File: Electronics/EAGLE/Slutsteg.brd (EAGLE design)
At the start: 100 x 160 mm, 167 parts, among them CN1 OSTYK33102030-2, CN2 OSTYK33102030-2, CN3 OSTYK33102030-2, IC1 SPX1117M3-L-3-3_TR, IC10 LM324D, IC11 L78M12ABDT-TR, IC2 L78M12ABDT-TR, IC3 ESP32-WROVER-IE-4MB, IC4 TM8211, IC5 LM324D, IC6 TPA3244DDWR, IC7 TPA3251D2DDVR, IC8 LM324D, IC9 LM324D, J1 0532610671, J2 JW-PJ-307-4H, J4 B4P-VH_LF__SN_, SW3 PDB181-K420F-103A2

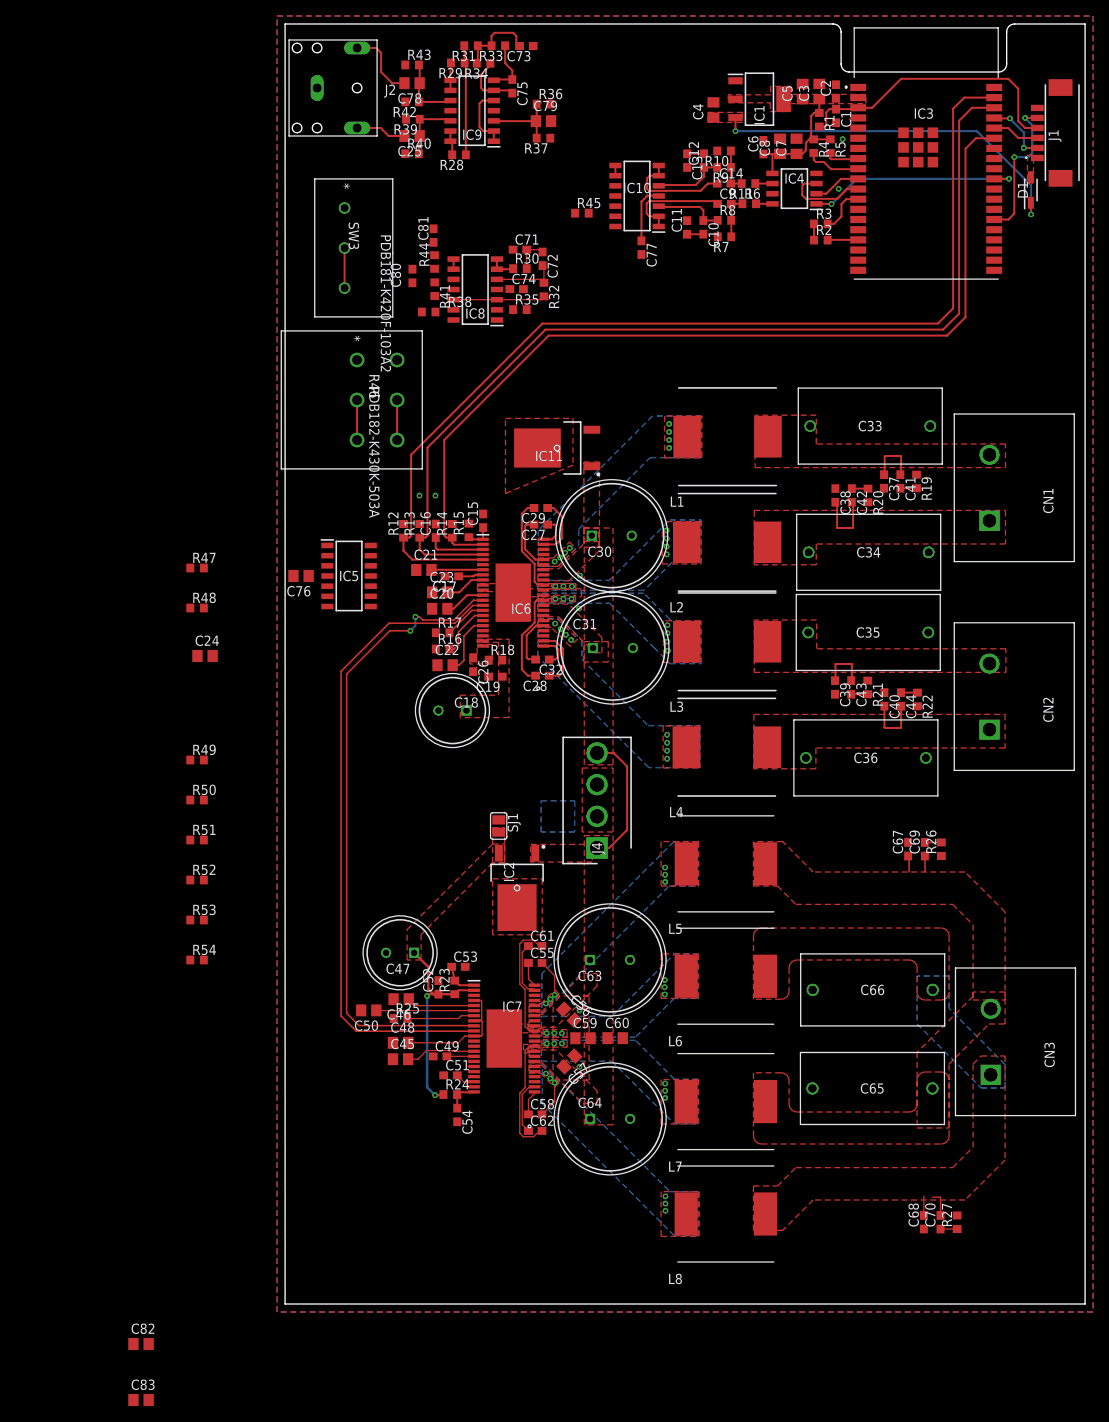
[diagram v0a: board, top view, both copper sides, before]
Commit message: Almost done with first draft of layout.
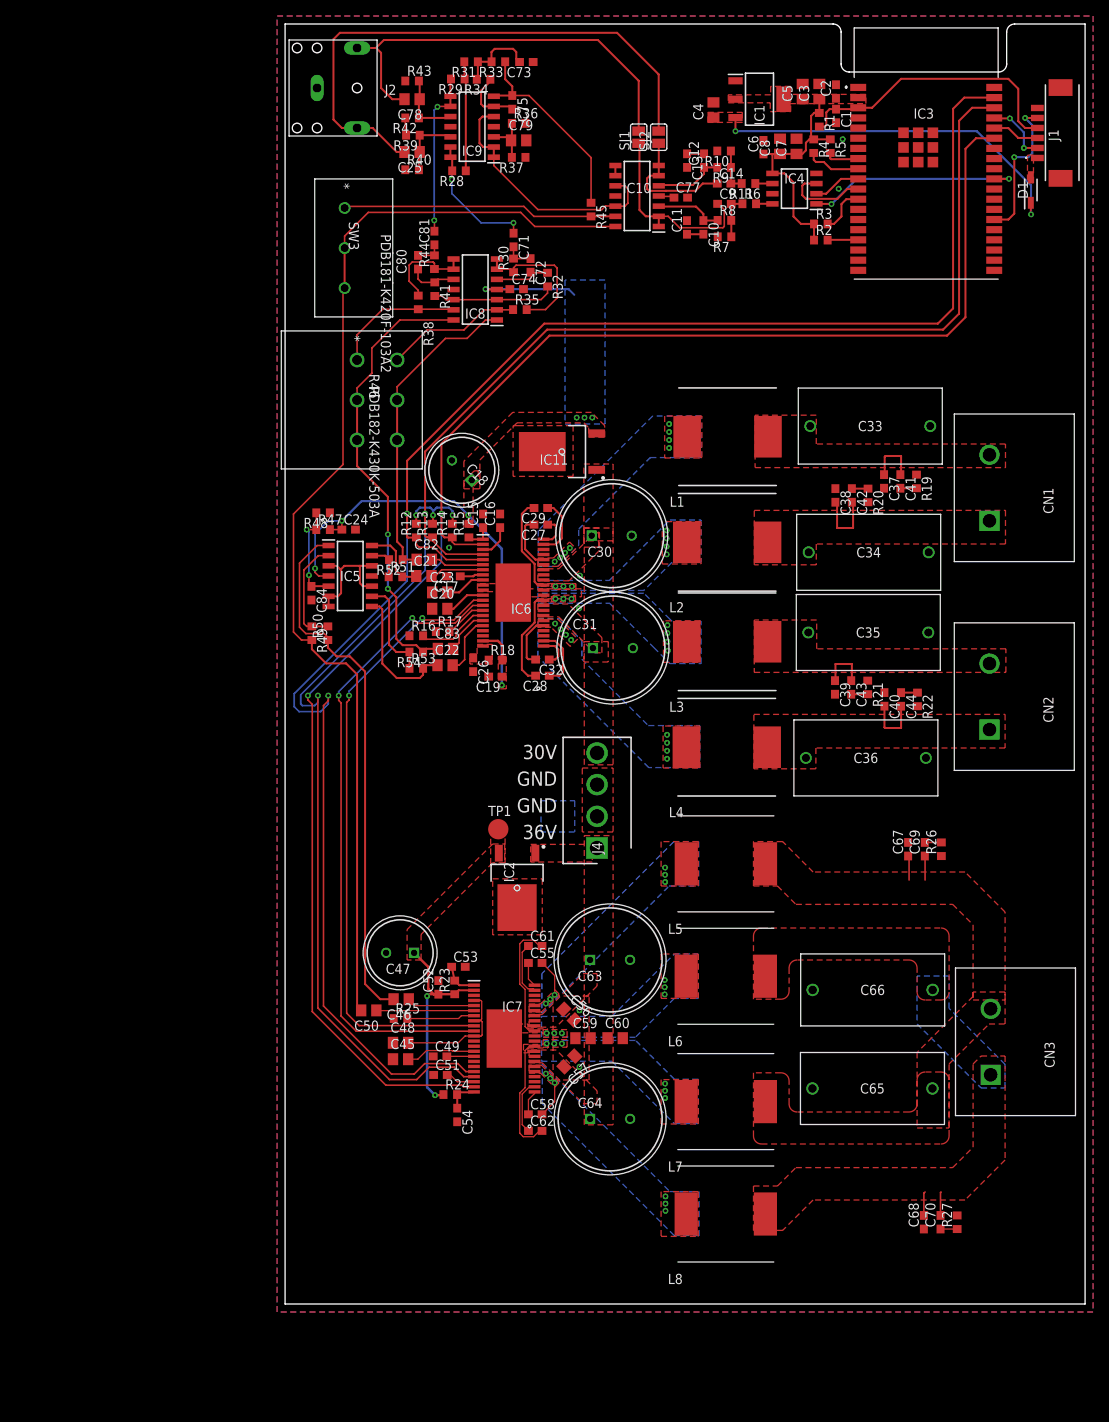
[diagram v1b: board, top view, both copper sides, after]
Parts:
- removed C76: 1uF/50V, rcl:C0805
- added C84: 100nF/50V, rcl:C0603
- added SJ2: (no value), jumper:SJ
- added TP1: TPB2,54, testpad:B2,54
- C24: value 1uF/50V -> 100nF/50V; device rcl:C0805 -> rcl:C0603
- moved C82 104.2 mm to (17.4, 93.0)
- moved C83 101.3 mm to (20.1, 81.9)
- moved SJ1 87.9 mm to (44.2, 145.8), turned to 90 degrees
- moved R54 47.3 mm to (16.4, 81.5), turned to 180 degrees
- moved R52 47.1 mm to (13.8, 93.0), turned to 180 degrees
- moved R53 41.7 mm to (16.4, 79.5)
- moved R51 41.2 mm to (13.8, 90.9)
- moved C18 28.8 mm to (23.3, 103.0), turned to 135 degrees
- moved R50 26.5 mm to (5.35, 83.8), turned to 90 degrees
- moved C24 23.9 mm to (7.95, 96.8)
- moved R49 21.4 mm to (3.35, 83.8), turned to 270 degrees
- moved R48 19.7 mm to (4.75, 98.9), turned to 180 degrees
- moved R47 16.5 mm to (4.75, 96.8)
- moved C16 8.15 mm to (26.9, 97.9)
- moved C77 7.96 mm to (49.5, 138.3), turned to 0 degrees
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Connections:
- removed net BASE_OUT: IC10.14, R49.2, SW3.2, SW3.3
- removed net BASE_OUT2: IC5.1, R50.1
- removed net BLE-L: C14.1, IC10.6, IC10.7
- removed net BLE-R: C9.1, IC10.1, IC10.2
- removed net LEFT_OUT: IC8.1, R46.5, R46.6, R52.1
- removed net LEFT_OUT2: IC5.14, R51.2
- removed net RIGHT_OUT: IC8.14, R46.2, R46.3, R54.1
- removed net RIGHT_OUT2: IC5.8, R53.2
- new net GSDJT: C9.1, IC10.1, IC10.2, SJ1.1
- new net PVDD2: C56.1, C57.2, C59.2, C60.1, C63.1, C64.1, IC2.1, IC7.29, IC7.30, IC7.31, IC7.36, IC7.37, IC7.38, J4.1
- new net TGHJESYRJK: C14.1, IC10.6, IC10.7, SJ2.1
- net GND: now also C84.2; no longer C76.2
- net INPUT_A: now also IC5.8, R53.2
- net INPUT_A_SLAVE: now also IC5.1, R50.1
- net INPUT_B: now also IC8.14, R46.2, R46.3, R54.1
- net INPUT_B_SLAVE: now also IC10.14, R49.2, SW3.2, SW3.3
- net INPUT_C: now also IC5.14, R51.2
- net INPUT_D: now also IC8.1, R46.5, R46.6, R52.1
- net N$6: now also C84.1; no longer C24.1
- net PVDD: no longer C56.1, C57.2, C59.2, C60.1, C63.1, C64.1, IC2.1, IC7.29, IC7.30, IC7.31, IC7.36, IC7.37, IC7.38, J4.1
- net SIG_IN_LEFT: now also SJ2.2
- net SIG_IN_RIGHT: now also SJ1.2
- net VDD: now also C24.1; no longer C76.1, SJ1.1
- net VDD2: now also TP1.TP; no longer SJ1.2
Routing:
- net INPUT_B_SLAVE: track 0.00 -> 141.0 mm
- net RESET: track 129.2 -> 225.8 mm, vias 0 -> 2
- net FAULT: track 124.3 -> 218.9 mm, vias 0 -> 2
- net CLIP_OTW: track 114.3 -> 208.1 mm, vias 0 -> 2
- net VDD: track 53.9 -> 124.9 mm, vias 2 -> 10
- net INPUT_A_SLAVE: track 0.00 -> 67.2 mm
- net SIG_IN_LEFT: track 6.34 -> 70.8 mm
- net INPUT_B: track 0.00 -> 56.9 mm, vias 0 -> 2
- net SIG_IN_RIGHT: track 9.15 -> 52.8 mm
- net INPUT_D: track 0.00 -> 39.6 mm
- net N$4: track 0.00 -> 34.4 mm
- net 6V_BUFFER: track 19.6 -> 47.6 mm
- net GSDJT: track 0.00 -> 24.5 mm
- net +3V3: track 20.4 -> 40.9 mm, vias 0 -> 3
- net BASE_VOLUME: track 6.93 -> 25.6 mm
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- added copper zone on layer 1, net PVDD2
- added copper zone on layer 16, net VDD
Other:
- board text added: "30V"
- board text added: "36V"
- board text added: "GND"

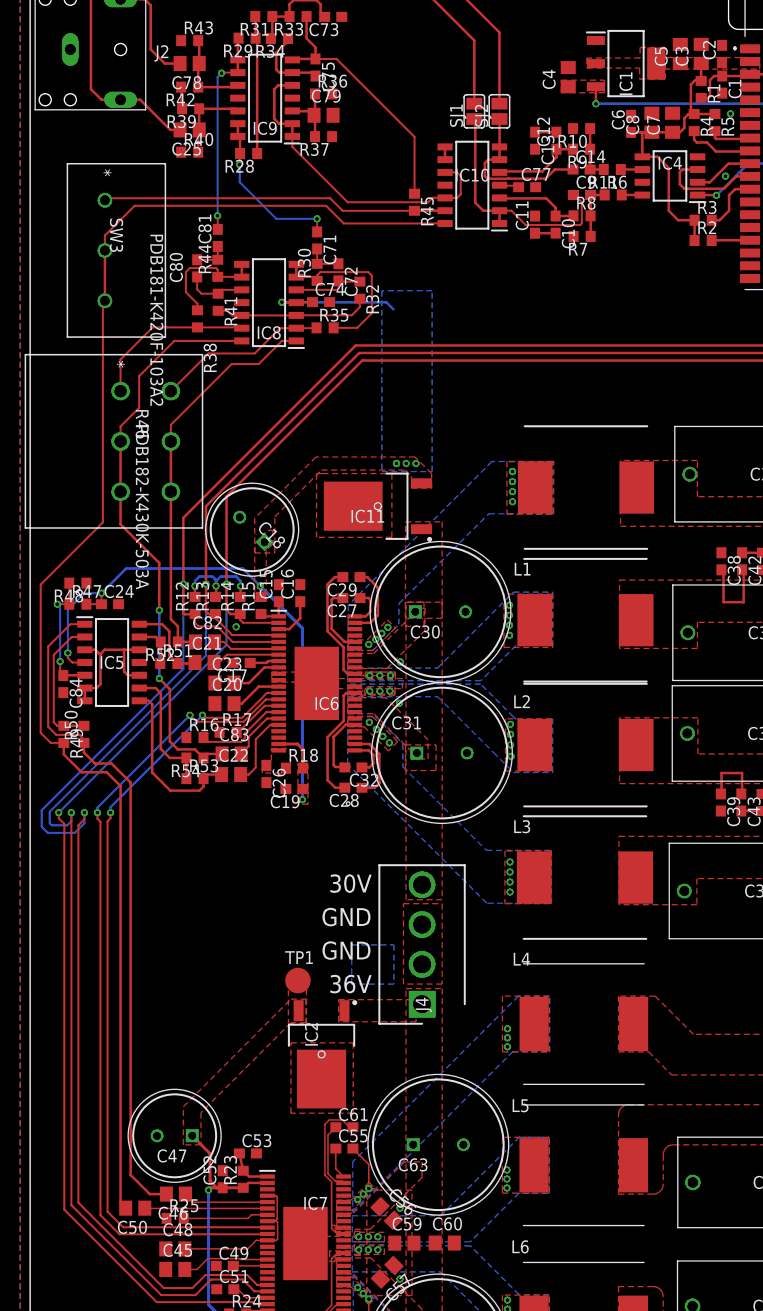
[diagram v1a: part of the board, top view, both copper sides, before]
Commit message: First draft of layout is finished. No DRC warnings.
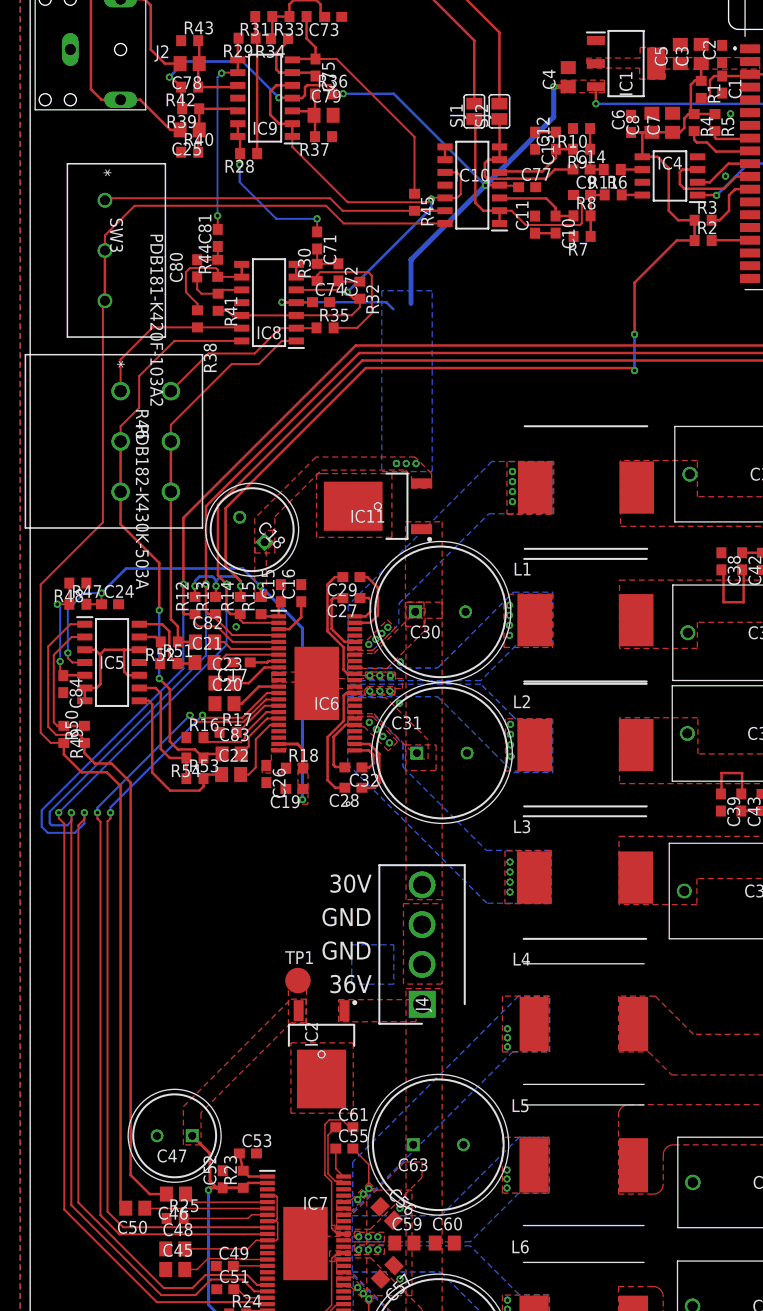
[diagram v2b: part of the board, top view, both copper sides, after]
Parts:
- moved C15 0.20 mm to (24.9, 97.9)
- moved C16 0.10 mm to (27.0, 97.9)
- moved C17 0.05 mm to (21.1, 91.0)
- moved R50 0.05 mm to (5.40, 83.8)
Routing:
- net +3V3: track 40.9 -> 112.2 mm, vias 3 -> 5
- net VDD: track 124.9 -> 195.7 mm, vias 10 -> 15
- net 6V_BUFFER: track 47.6 -> 62.3 mm, vias 0 -> 2
- net CLIP_OTW: track 208.1 -> 208.8 mm

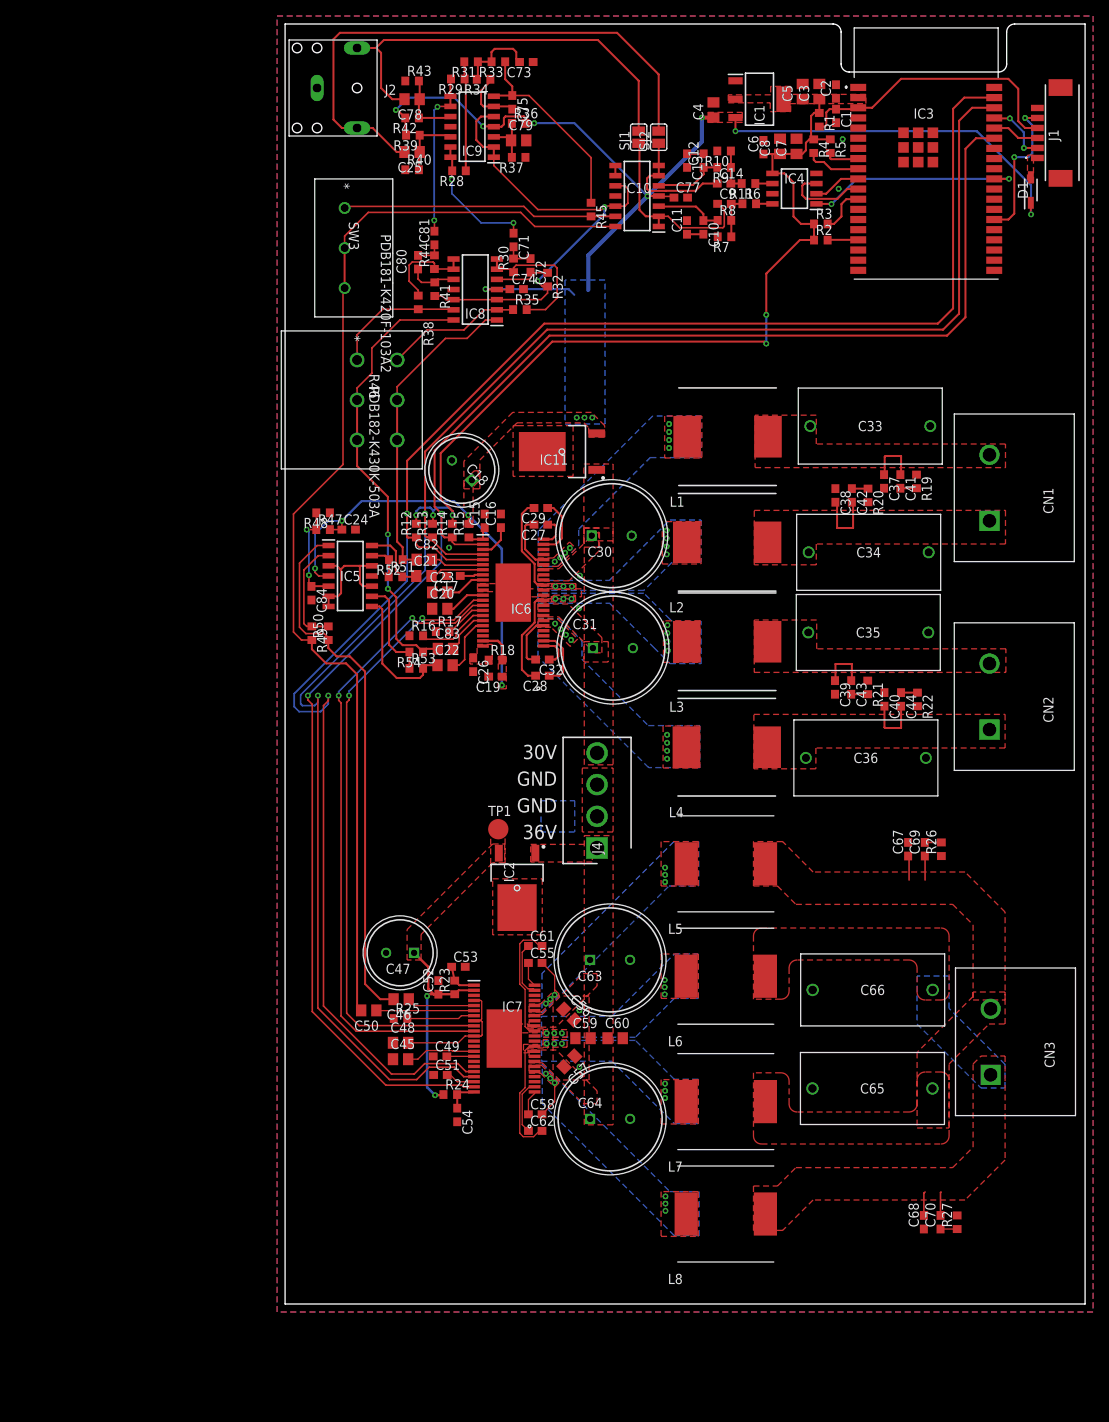
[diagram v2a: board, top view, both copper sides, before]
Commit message: Added some test points. More to come....
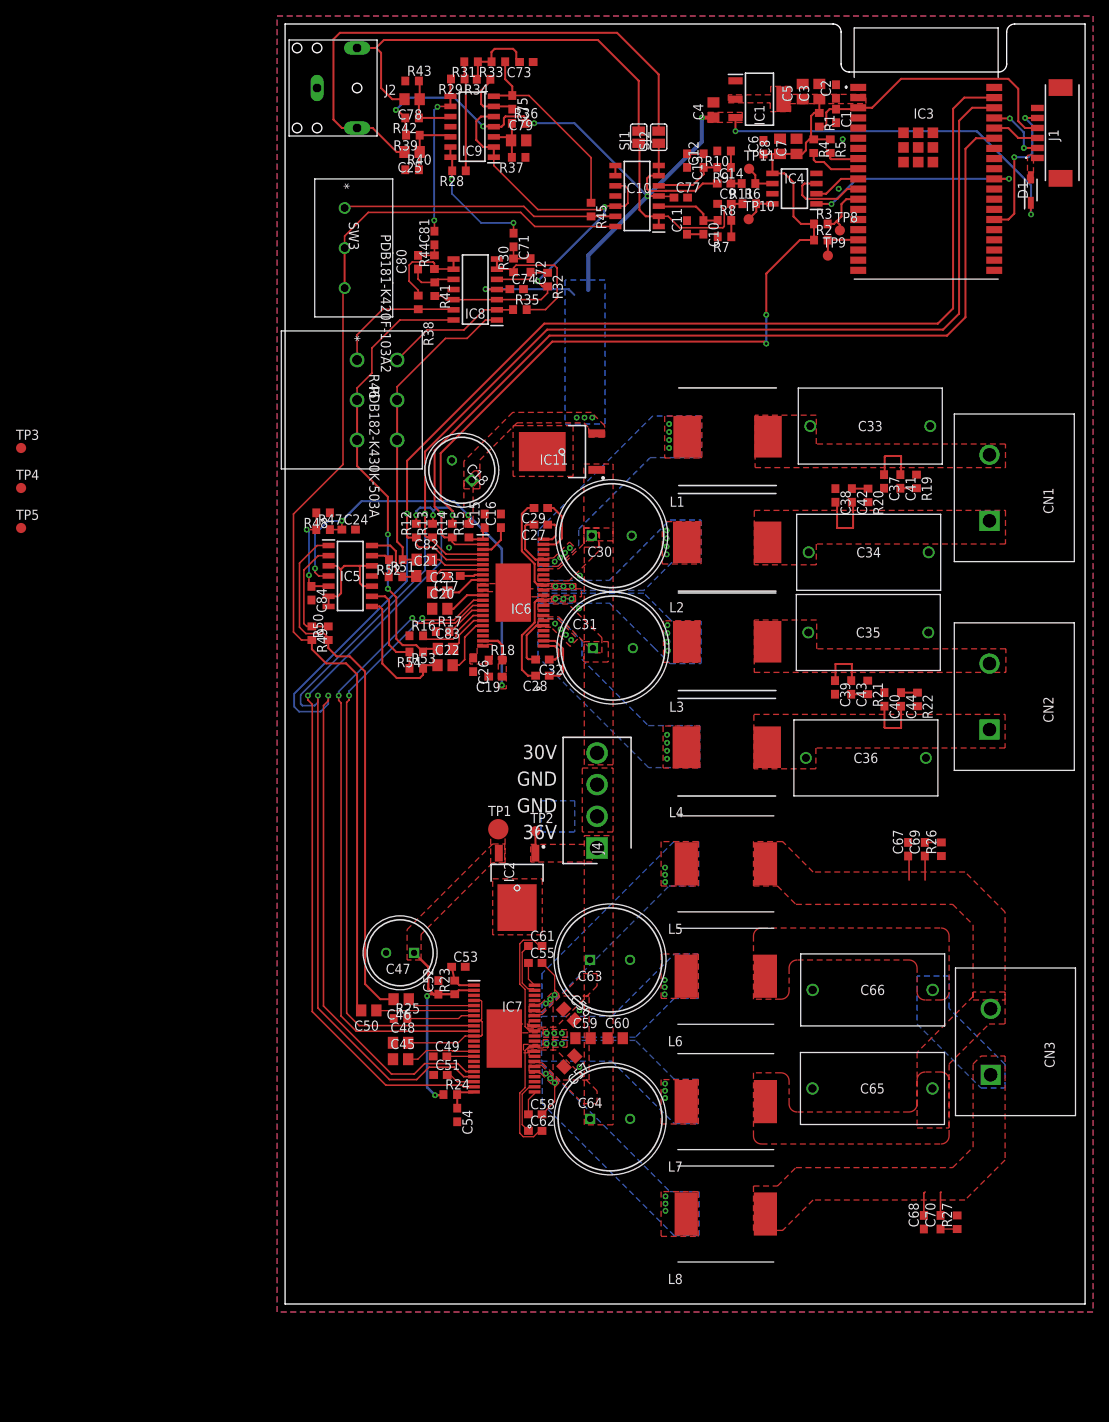
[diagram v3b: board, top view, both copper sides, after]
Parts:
- added TP10, TP11, TP2, TP3, TP4, TP5, TP8, TP9: TPB1,27, testpad:B1,27
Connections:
- net +3V3: now also TP4.TP
- net DAC-L_N: now also TP11.TP
- net DAC-R_P: now also TP10.TP
- net NEXT: now also TP8.TP
- net PREV: now also TP9.TP
- net PVDD: now also TP3.TP
- net PVDD2: now also TP2.TP
- net VDD: now also TP5.TP
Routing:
- net PVDD2: track 0.00 -> 2.76 mm
- net DAC-R_P: track 2.06 -> 4.38 mm
- net DAC-L_N: track 2.14 -> 4.31 mm
- net PREV: track 3.83 -> 5.78 mm
- net NEXT: track 6.01 -> 7.31 mm
